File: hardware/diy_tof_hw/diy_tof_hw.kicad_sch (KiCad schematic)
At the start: 1 part, among them U1 NUCLEO-F042K6

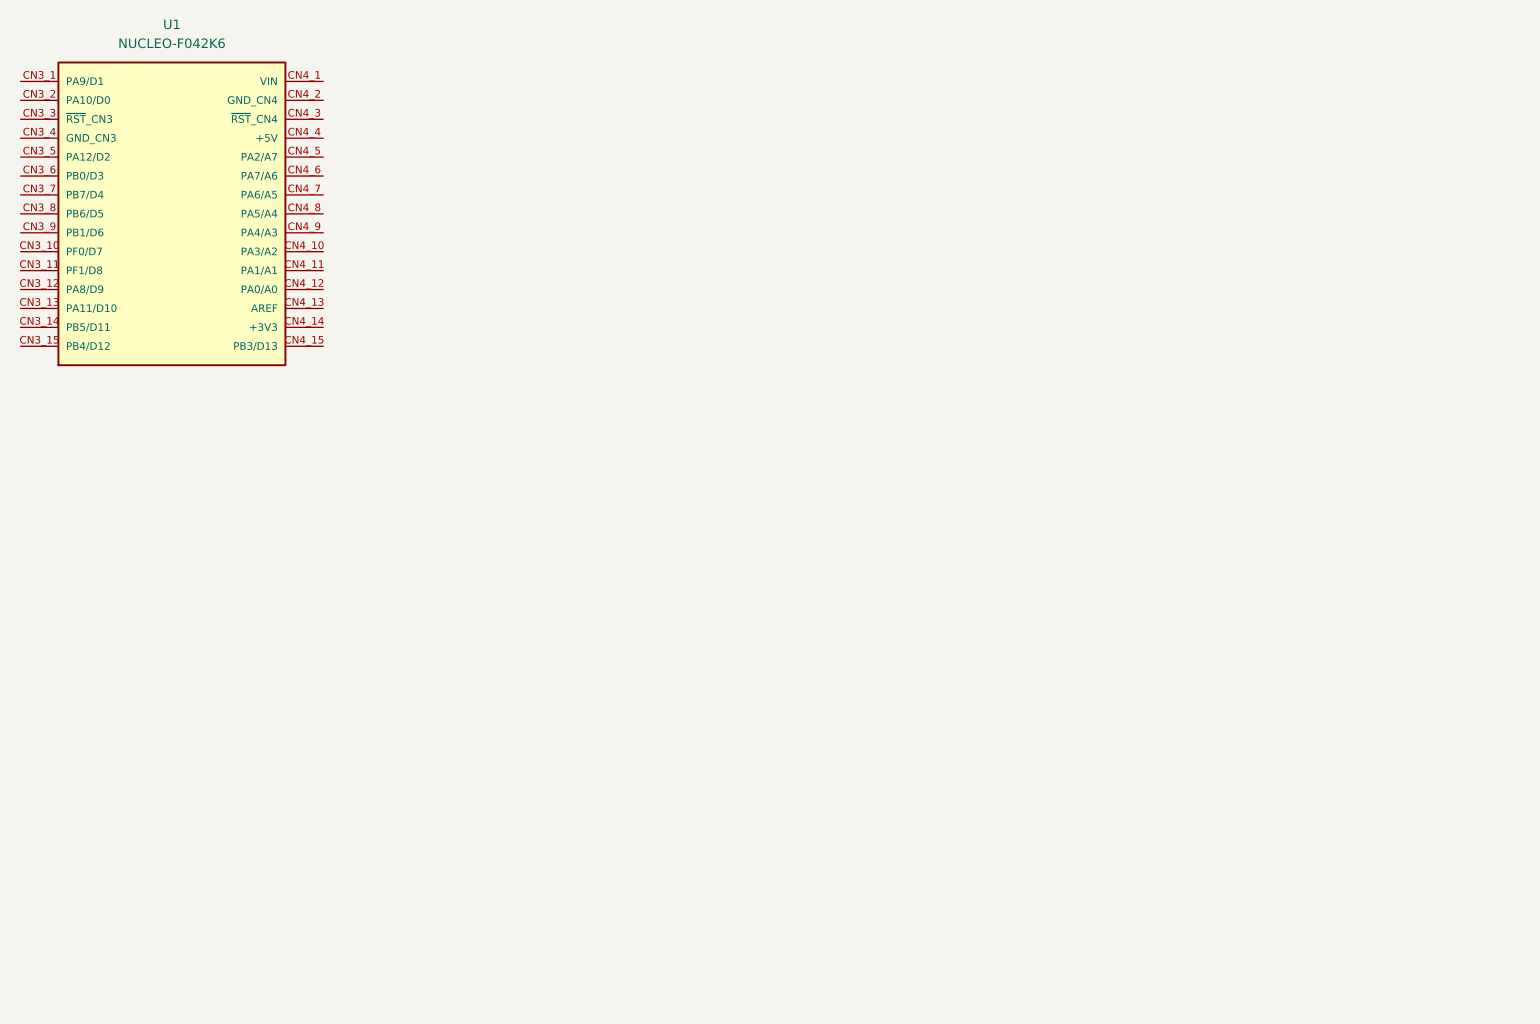
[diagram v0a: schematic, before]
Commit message: [hardware] wip - added two new schematics for better hierarchy, started to place power input plugs and power selection jumpers
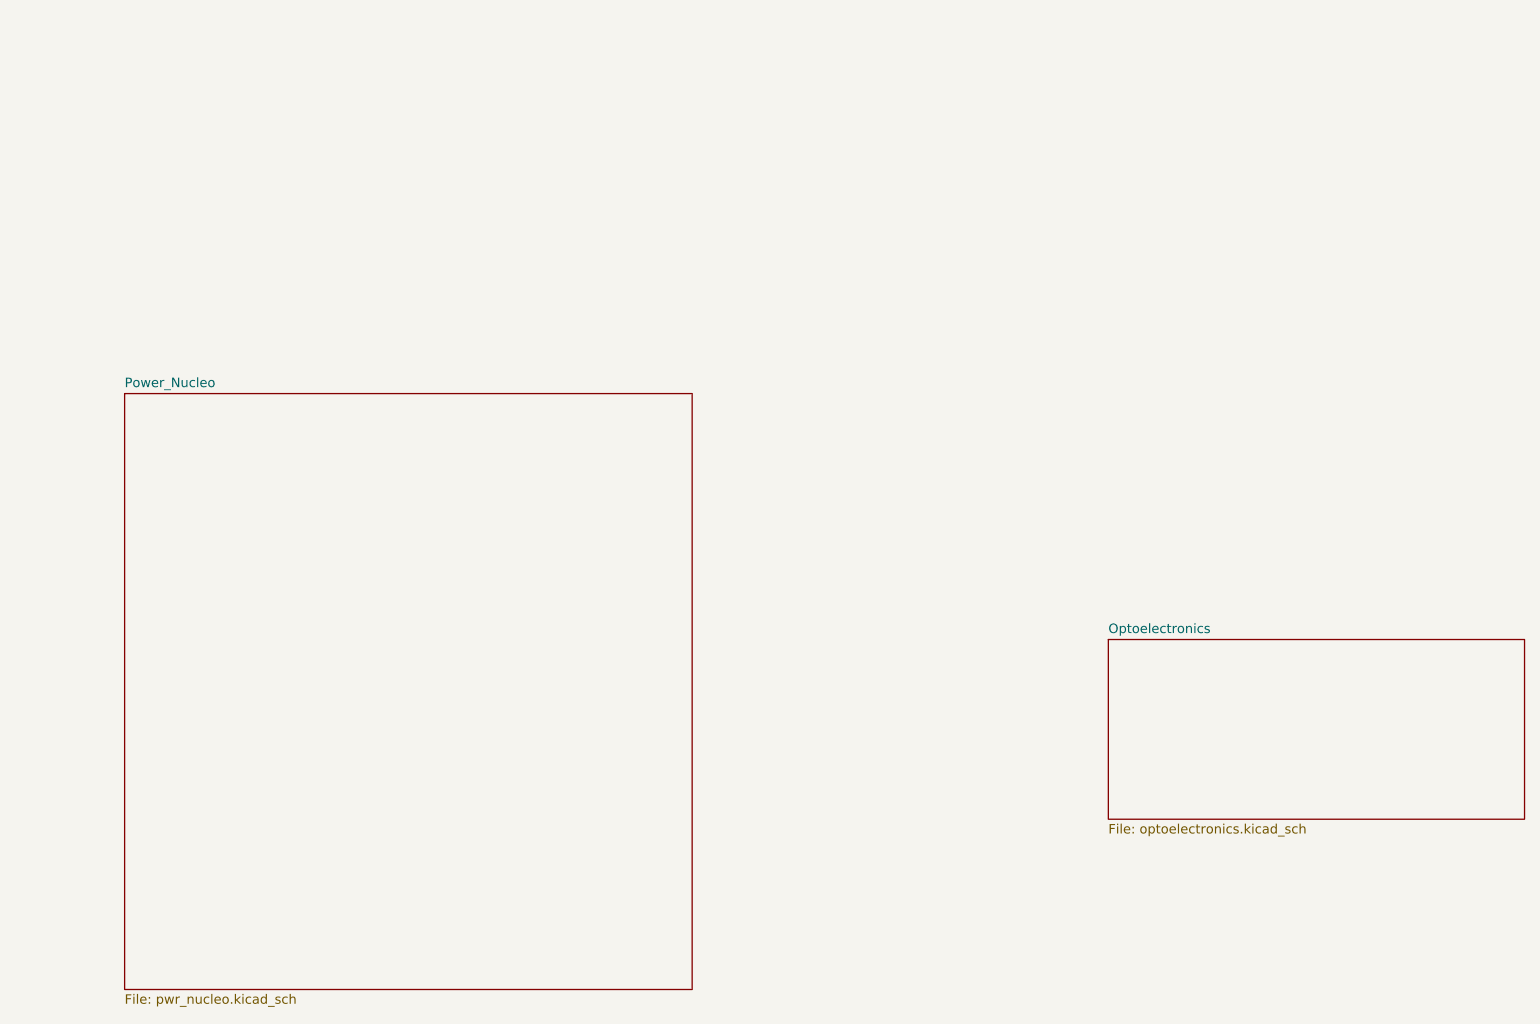
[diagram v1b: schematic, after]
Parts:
- removed U1: NUCLEO-F042K6, NUCLEO_F042K6:MODULE_NUCLEO-F042K6, symbol NUCLEO-F042K6:NUCLEO-F042K6
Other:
- added sheet Optoelectronics (optoelectronics.kicad_sch)
- added sheet Power_Nucleo (pwr_nucleo.kicad_sch)
- company: (none) -> OST
- title: (none) -> PCB DIY ToF
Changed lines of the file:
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@@
 	(generator "eeschema")
 	(generator_version "8.0")
-	(paper "A4")
-	(symbol
-		(lib_id "NUCLEO-F042K6:NUCLEO-F042K6")
-		(at 67.31 55.88 0)
-		(unit 1)
-		(exclude_from_sim no)
-		(in_bom yes)
-		(on_board yes)
-		(dnp no)
+	(paper "A3")
+	(title_block
+		(title "PCB DIY ToF")
+		(date "2024-12-21")
+		(rev "0.1")
+		(company "OST")
+		(comment 1 "Top level")
+		(comment 2 "schematics")
+		(comment 3 "w.i.p.")
+		(comment 8 "M. Schär")
+	)
+	(sheet
+		(at 193.04 113.03)
+		(size 55.88 24.13)
 		(fields_autoplaced yes)
-		(property "Reference" "U1"
-			(at 67.31 30.48 0)
+		(stroke
+			(width 0.1524)
+			(type solid)
+		)
+		(fill
+			(color 0 0 0 0.0000)
+		)
+		(property "Sheetname" "Optoelectronics"
+			(at 193.04 112.3184 0)
 			(effects
 				(font
 					(size 1.27 1.27)
 				)
+				(justify left bottom)
 			)
 		)
-		(property "Value" "NUCLEO-F042K6"
-			(at 67.31 33.02 0)
+		(property "Sheetfile" "optoelectronics.kicad_sch"
+			(at 193.04 137.7446 0)
 			(effects
 				(font
 					(size 1.27 1.27)
 				)
+				(justify left top)
 			)
 		)
-		(property "Footprint" "NUCLEO_F042K6:MODULE_NUCLEO-F042K6"
-			(at 67.31 55.88 0)
+		(instances
+			(project "diy_tof_hw"
+				(path "/0f7bf370-0a80-4101-a61d-d850fd66ab1d"
+					(page "3")
+				)
+			)
+		)
+	)
+	(sheet
+		(at 60.96 80.01)
+		(size 76.2 80.01)
+		(fields_autoplaced yes)
+		(stroke
+			(width 0.1524)
+			(type solid)
+		)
+		(fill
+			(color 0 0 0 0.0000)
+		)
+		(property "Sheetname" "Power_Nucleo"
+			(at 60.96 79.2984 0)
 			(effects
 				(font
 					(size 1.27 1.27)
 				)
-				(justify bottom)
-				(hide yes)
+				(justify left bottom)
 			)
 		)
-		(property "Datasheet" ""
-			(at 67.31 55.88 0)
+		(property "Sheetfile" "pwr_nucleo.kicad_sch"
+			(at 60.96 160.6046 0)
 			(effects
 				(font
 					(size 1.27 1.27)
 				)
-				(hide yes)
+				(justify left top)
 			)
 		)
-		(property "Description" ""
-			(at 67.31 55.88 0)
-			(effects
-				(font
-					(size 1.27 1.27)
-				)
-				(hide yes)
-			)
-		)
-		(property "PARTREV" "8"
-			(at 67.31 55.88 0)
-			(effects
-				(font
-					(size 1.27 1.27)
-				)
-				(justify bottom)
-				(hide yes)
-			)
-		)
-		(property "STANDARD" "Manufacturer Recommendations"
-			(at 67.31 55.88 0)
-			(effects
-				(font
-					(size 1.27 1.27)
-				)
-				(justify bottom)
-				(hide yes)
-			)
-		)
-		(property "MAXIMUM_PACKAGE_HEIGHT" "14.5mm"
-			(at 67.31 55.88 0)
-			(effects
-				(font
-					(size 1.27 1.27)
-				)
-				(justify bottom)
-				(hide yes)
-			)
-		)
-		(property "MANUFACTURER" "STMicroelectronics"
-			(at 67.31 55.88 0)
-			(effects
-				(font
-					(size 1.27 1.27)
-				)
-				(justify bottom)
-				(hide yes)
-			)
-		)
-		(pin "CN3_14"
-		)
-		(pin "CN4_15"
-		)
-		(pin "CN4_8"
-		)
-		(pin "CN4_2"
-		)
-		(pin "CN4_13"
-		)
-		(pin "CN4_14"
-		)
-		(pin "CN3_3"
-		)
-		(pin "CN3_10"
-		)
-		(pin "CN4_7"
-		)
-		(pin "CN3_5"
-		)
-		(pin "CN3_11"
-		)
-		(pin "CN3_12"
-		)
-		(pin "CN3_8"
-		)
-		(pin "CN4_5"
-		)
-		(pin "CN4_3"
-		)
-		(pin "CN4_9"
-		)
-		(pin "CN3_7"
-		)
-		(pin "CN3_4"
-		)
-		(pin "CN3_6"
-		)
-		(pin "CN3_9"
-		)
-		(pin "CN4_1"
-		)
-		(pin "CN4_6"
-		)
-		(pin "CN3_2"
-		)
-		(pin "CN4_4"
-		)
-		(pin "CN3_13"
-		)
-		(pin "CN3_1"
-		)
-		(pin "CN4_10"
-		)
-		(pin "CN4_12"
-		)
-		(pin "CN4_11"
-		)
-		(pin "CN3_15"
-		)
 		(instances
-			(project ""
+			(project "diy_tof_hw"
 				(path "/0f7bf370-0a80-4101-a61d-d850fd66ab1d"
-					(reference "U1")
-					(unit 1)
+					(page "2")
 				)
 			)

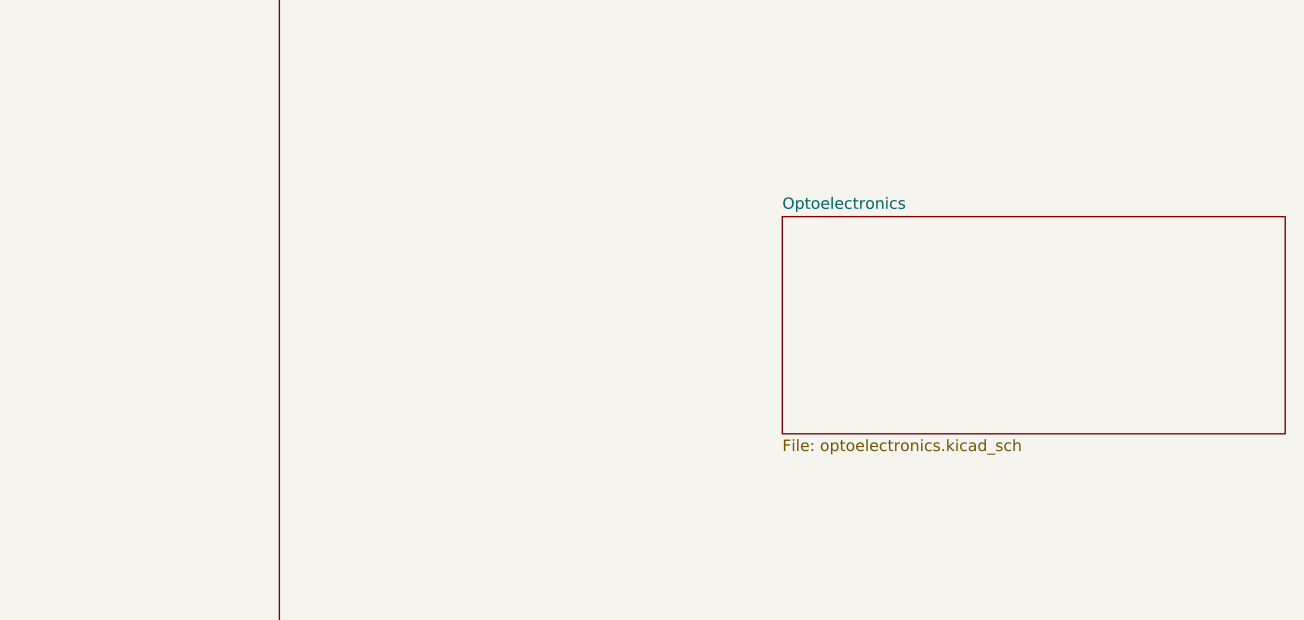
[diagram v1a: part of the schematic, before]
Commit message: [hardware] drawn initial version of the power / nucleo sheet
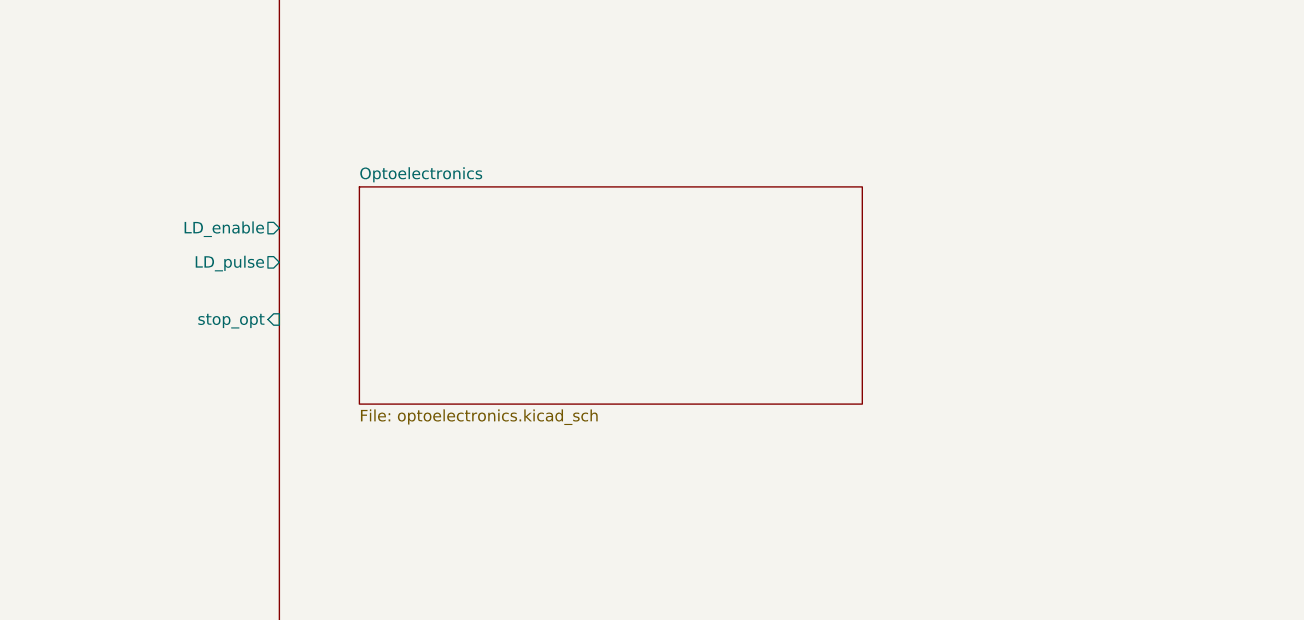
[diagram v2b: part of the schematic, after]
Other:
- sheet Power_Nucleo ports: added LD_enable, LD_pulse, stop_opt; removed none
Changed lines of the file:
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@@
 	)
 	(sheet
-		(at 193.04 113.03)
+		(at 146.05 109.728)
 		(size 55.88 24.13)
 		(fields_autoplaced yes)
@@
 		)
 		(property "Sheetname" "Optoelectronics"
-			(at 193.04 112.3184 0)
+			(at 146.05 109.0164 0)
 			(effects
 				(font
@@
 		)
 		(property "Sheetfile" "optoelectronics.kicad_sch"
-			(at 193.04 137.7446 0)
+			(at 146.05 134.4426 0)
 			(effects
 				(font
@@
 			)
 		)
+		(pin "LD_pulse" output
+			(at 137.16 118.11 0)
+			(effects
+				(font
+					(size 1.27 1.27)
+				)
+				(justify right)
+			)
+		)
+		(pin "stop_opt" input
+			(at 137.16 124.46 0)
+			(effects
+				(font
+					(size 1.27 1.27)
+				)
+				(justify right)
+			)
+		)
+		(pin "LD_enable" output
+			(at 137.16 114.3 0)
+			(effects
+				(font
+					(size 1.27 1.27)
+				)
+				(justify right)
+			)
+		)
